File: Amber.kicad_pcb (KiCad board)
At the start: 4 copper layers, 120 x 120 mm, 305 parts, among them J1 Barrel_Jack, J11 Conn_02x05_Odd_Even, J12 Bus_M.2_Socket_M, J13 Conn_01x03_Male, J2 RJ45_LINK-PP_LPJG0926HENL_Hor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, J3 USB_C_Receptacle_USB2.0, J4 USB_A_Stacked, J5 AudioJack, J6 HDMI_D_2.0, J7 Micro_SD_Card_Det, J8 SiLabs Mini Debug, J9 Conn_Coaxial, M1 Fan_4pin, Q1 DMP3013SFV-7, Q2 BSZ440N10NS3GATMA1, Q3 MMBTA06, Q4 BC817, SW1 SW_USER, SW2 SW_WIPE, T1 PA2467NL, U1 RaspberryPi-CM4Lite, U10 TPD4EUSB30, U11 SiliconLabs-MGM210P, U12 PCM5121PW, U13 TLV74033PDBVR, U14 TPD4EUSB30, U15 TPD4EUSB30, U16 BD9D321EFJ, U17 BD9D321EFJ, U18 74LVC1G07, U19 74LVC1G07, U2 DF40C-100DS-0.4V, U20 LP5569RTWR, U21 PCF85063AT, U22 RT9742GGJ5, U23 MP8008, U24 TCMT1107, U25 PCF8563TS, U26 74LVC1G07, U27 74LVC1G07, U28 TCMT1107, U29 TL431DBZ, U3 DF40C-100DS-0.4V, U4 CP2102N-Axx-xQFN24, U5 FSUSB30MUX, U6 FSUSB30MUX, U7 FE1.1, U8 TPD4EUSB30, U9 AP2191W, Y1 12MHz/10pF, Y2 32768Hz/12.5pF

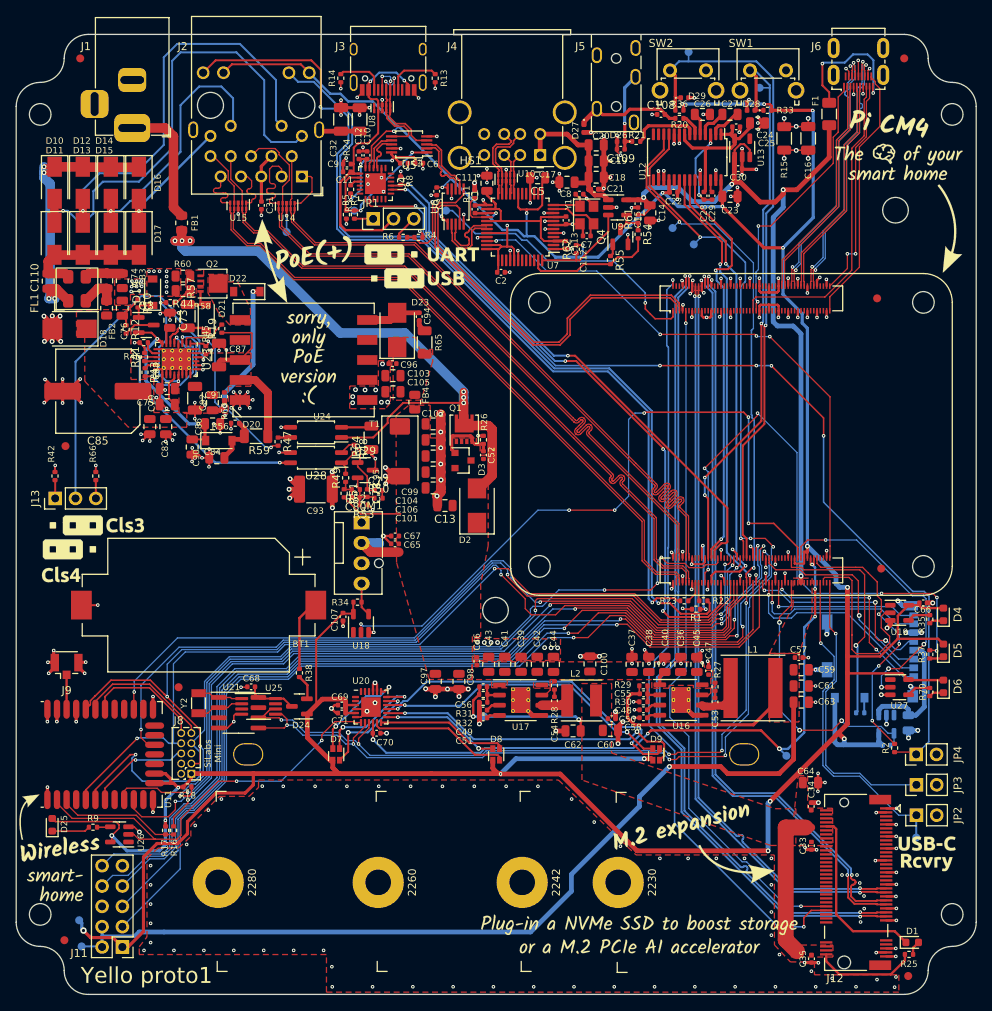
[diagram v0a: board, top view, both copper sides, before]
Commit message: Fix FSUSB30 Symbol and routing
Additionally a cap was added to U27.

Signed-off-by: Dominik Sliwa <dominik@sliwa.io>
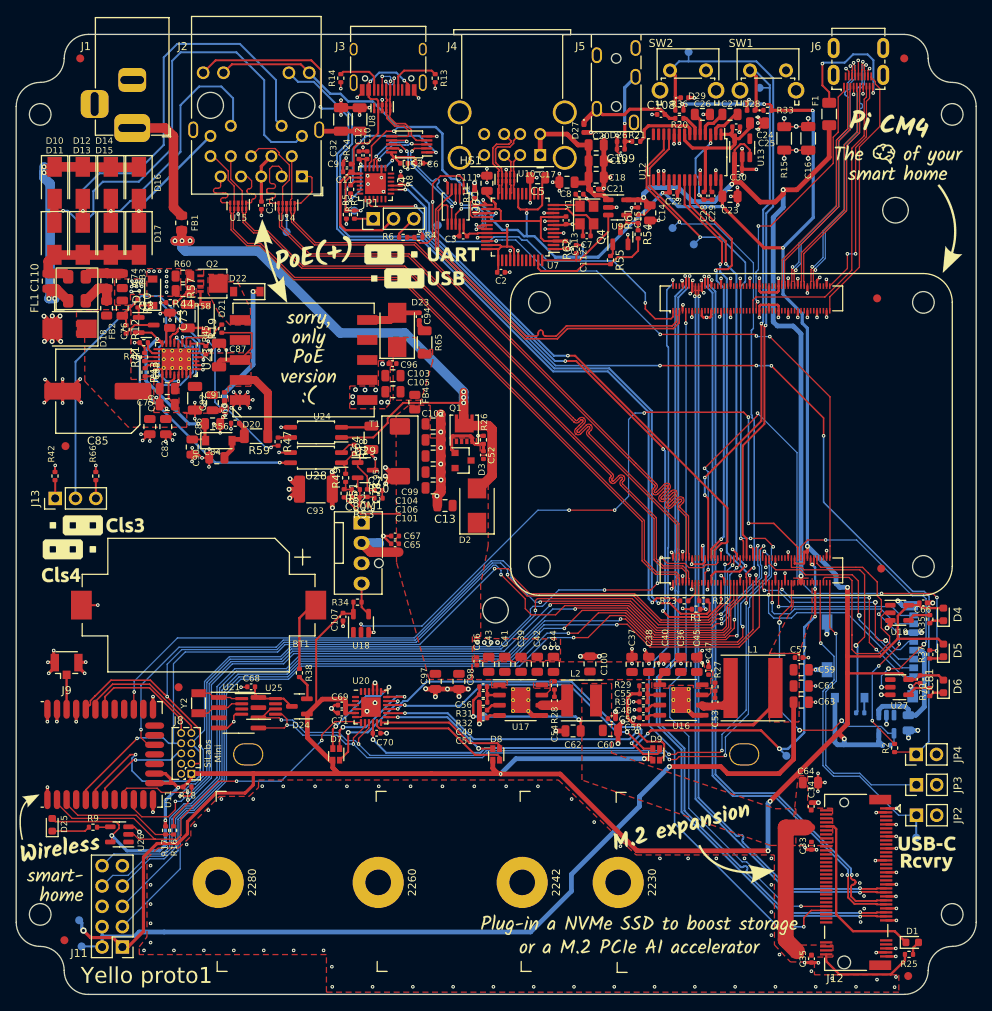
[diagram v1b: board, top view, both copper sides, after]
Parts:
- added C81: 100n, Capacitor_SMD:C_0402_1005Metric, F.Cu at (143.0, 110.6)
- moved C3 6.50 mm to (85.9, 55.2), turned to 180 degrees
- moved TP3 2.10 mm to (82.7, 53.9)
- turned U6 to -90 degrees
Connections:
- U5 pad 3: /USB/OTG.D- -> /USB/CP.D+
- U5 pad 8: /USB/CP.D+ -> /USB/OTG.D-
- U6 pad 3: /USB/HUB.D- -> /USB/OTG.D+
- U6 pad 8: /USB/OTG.D+ -> /USB/HUB.D-
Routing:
- net /USB/MUX2_SEL: track 20.1 -> 30.4 mm
- net /CM4/CM4_USB_OTG_ID: track 48.9 -> 57.3 mm, vias 3 -> 2
- net /USB/OTG.D-: track 8.16 -> 13.7 mm, vias 0 -> 2
- net /USB/OTG.D+: track 8.14 -> 13.7 mm, vias 0 -> 2
- net +3V3: track 521.0 -> 525.9 mm, vias 23 -> 22
- net /CM4/CM4_USB_D+: track 49.8 -> 45.9 mm
- net /CM4/CM4_USB_D-: track 49.8 -> 46.0 mm
- net /USB/CP.D+: track 5.10 -> 8.24 mm, vias 0 -> 2
- net /USB/CP.D-: track 5.09 -> 8.20 mm, vias 0 -> 2
- net GND: track 334.8 -> 336.9 mm, vias 322 -> 321
- net GND1: track 76.6 -> 75.9 mm, vias 50 -> 49
- net /USB/HUB.D+: track 8.87 -> 9.59 mm, vias 0 -> 2
- net /USB/HUB.D-: track 8.88 -> 9.54 mm, vias 0 -> 2
